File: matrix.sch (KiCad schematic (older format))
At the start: 143 parts

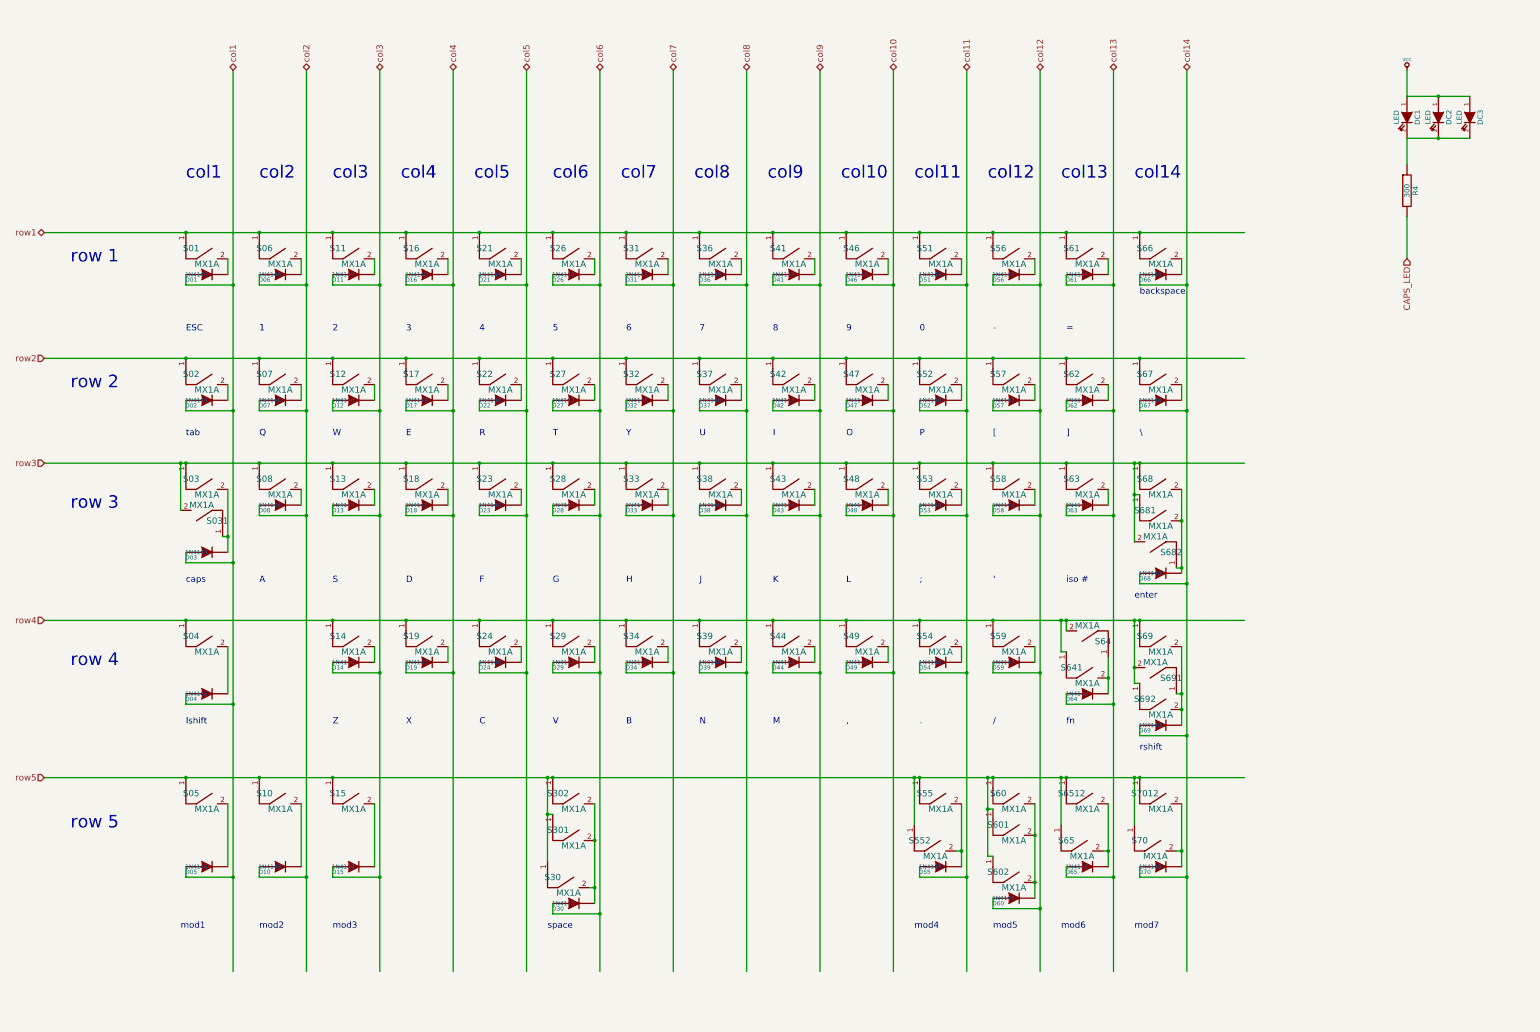
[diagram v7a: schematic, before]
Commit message: Remove unnecessary caps SW and related leds
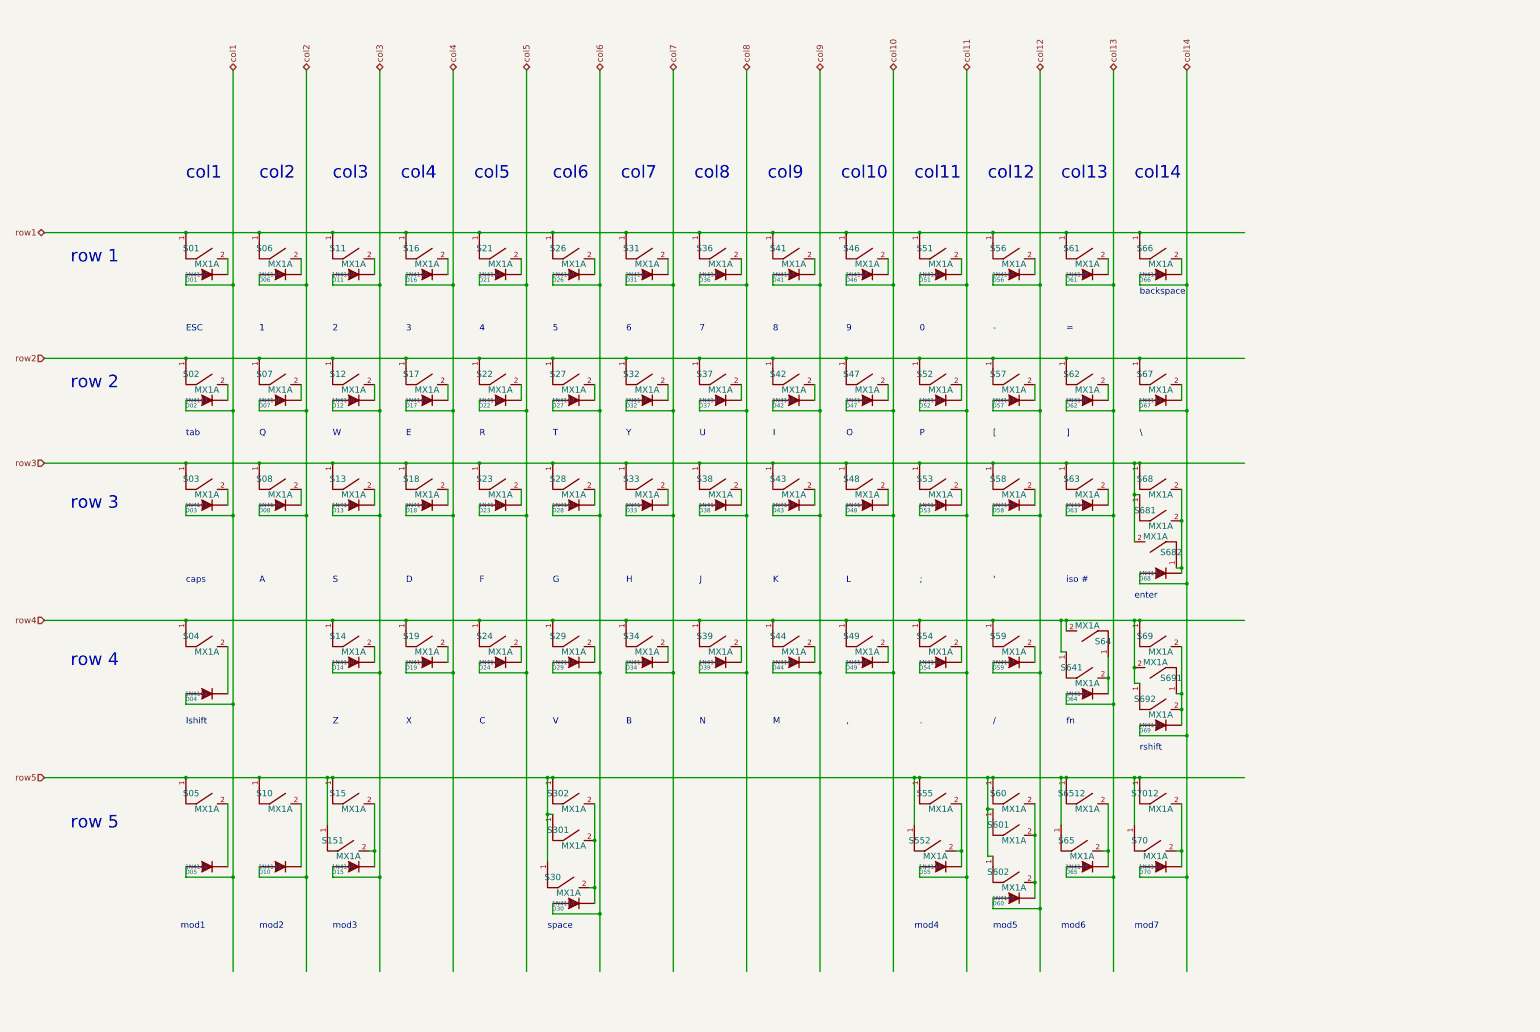
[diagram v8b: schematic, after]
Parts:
- removed DC1, DC2: LED, mx1a:MX1A-led_no3d, symbol device:LED
- removed DC3: LED, symbol device:LED
- removed R4: 300, symbol device:R
- removed S031: MX1A, mx1a:MX1A_no3d, symbol mx1a-simple:MX1A
- added S151: MX1A, mx1a:MX1A_no3d, symbol mx1a-simple:MX1A
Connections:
- net labels removed: CAPS_LED, VCC
- wire segments 390 -> 383
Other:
- moved on the sheet: D03
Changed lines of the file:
@@
 Text Notes 8000 2450 0    120  ~ 0
 col8
-$Comp
-L mx1a-simple:MX1A S031
-U 1 1 5042A9E4
-P 3300 5450
-F 0 "S031" H 3150 5700 60  0000 C CNN
-F 1 "MX1A" H 3300 5550 60  0000 C CNN
-F 2 "mx1a:MX1A_no3d" H 3300 5450 60  0001 C CNN
-F 3 "" H 3300 5450 60  0001 C CNN
-	1    3300 5450
-	-1   0    0    1
-$EndComp
-$Comp
-L device:LED DC1
-U 1 1 5042BB59
-P 14800 1850
-F 0 "DC1" H 14800 1950 50  0000 C CNN
-F 1 "LED" H 14800 1750 50  0000 C CNN
-F 2 "mx1a:MX1A-led_no3d" H 14800 1850 60  0001 C CNN
-F 3 "" H 14800 1850 60  0001 C CNN
-	1    14800 1850
-	0    1    1    0
-$EndComp
-$Comp
-L device:LED DC2
-U 1 1 5042BEB0
-P 15100 1850
-F 0 "DC2" H 15100 1950 50  0000 C CNN
-F 1 "LED" H 15100 1750 50  0000 C CNN
-F 2 "mx1a:MX1A-led_no3d" H 15100 1850 60  0001 C CNN
-F 3 "" H 15100 1850 60  0001 C CNN
-	1    15100 1850
-	0    1    1    0
-$EndComp
 Text HLabel 1800 2950 0    60   3State ~ 0
 row1
@@
 col14
 $Comp
-L power1:VCC #PWR031
-U 1 1 5043970C
-P 14800 1400
-F 0 "#PWR031" H 14800 1500 30  0001 C CNN
-F 1 "VCC" H 14800 1500 30  0000 C CNN
-F 2 "" H 14800 1400 60  0001 C CNN
-F 3 "" H 14800 1400 60  0001 C CNN
-	1    14800 1400
-	1    0    0    -1
-$EndComp
-$Comp
-L device:R R4
-U 1 1 5043A0D0
-P 14800 2550
-F 0 "R4" V 14880 2550 50  0000 C CNN
-F 1 "300" V 14800 2550 50  0000 C CNN
-F 2 "" H 14800 2550 60  0001 C CNN
-F 3 "" H 14800 2550 60  0001 C CNN
-	1    14800 2550
-	1    0    0    -1
-$EndComp
-Text HLabel 14800 3200 3    60   Input ~ 0
-CAPS_LED
-$Comp
 L mx1a-simple:MX1A S41
 U 1 1 5040DDC7
@@
 L device:DIODE D03
 U 1 1 506B5DE9
-P 3350 6000
-F 0 "D03" H 3200 5950 40  0000 C CNN
-F 1 "1N4148" H 3250 6000 40  0000 C CNN
-F 2 "0805:0805D" H 3350 6000 60  0001 C CNN
-F 3 "" H 3350 6000 60  0001 C CNN
-F 4 "DC Components" H 3350 4350 60  0001 C CNN "Vendor"
-F 5 "CD4148WS(0805C)" H 3350 4350 60  0001 C CNN "Product"
-F 6 "TME" H 3350 4350 60  0001 C CNN "Supplier"
-F 7 "1N4148-0805" H 3350 4350 60  0001 C CNN "Supplier Symbol"
-	1    3350 6000
-	1    0    0    -1
-$EndComp
-$Comp
-L device:LED DC3
-U 1 1 506E072F
-P 15400 1850
-F 0 "DC3" H 15400 1950 50  0000 C CNN
-F 1 "LED" H 15400 1750 50  0000 C CNN
-F 2 "" H 15400 1850 60  0001 C CNN
-F 3 "" H 15400 1850 60  0001 C CNN
-	1    15400 1850
-	0    1    1    0
+P 3350 5550
+F 0 "D03" H 3200 5500 40  0000 C CNN
+F 1 "1N4148" H 3250 5550 40  0000 C CNN
+F 2 "0805:0805D" H 3350 5550 60  0001 C CNN
+F 3 "" H 3350 5550 60  0001 C CNN
+F 4 "DC Components" H 3350 3900 60  0001 C CNN "Vendor"
+F 5 "CD4148WS(0805C)" H 3350 3900 60  0001 C CNN "Product"
+F 6 "TME" H 3350 3900 60  0001 C CNN "Supplier"
+F 7 "1N4148-0805" H 3350 3900 60  0001 C CNN "Supplier Symbol"
+	1    3350 5550
+	1    0    0    -1
 $EndComp
 $Comp
@@
 Connection ~ 11250 8700
 Wire Wire Line
-	1800 5150 3100 5150
-Wire Wire Line
 	5000 1400 5000 3450
 Wire Wire Line
@@
 Wire Wire Line
 	7050 9200 7000 9200
-Wire Wire Line
-	3100 5150 3100 5600
-Connection ~ 3100 5150
-Wire Wire Line
-	3550 5400 3550 5850
-Wire Wire Line
-	3550 5850 3500 5850
-Wire Wire Line
-	14800 1400 14800 1650
-Wire Wire Line
-	14800 1650 15100 1650
-Wire Wire Line
-	14800 2050 15100 2050
-Wire Wire Line
-	14800 2050 14800 2300
-Wire Wire Line
-	14800 2800 14800 3200
 Wire Wire Line
 	12200 6650 12200 7100
@@
 Connection ~ 7050 9200
 Wire Wire Line
-	3150 6000 3150 6100
-Wire Wire Line
-	3150 6100 3600 6100
+	3150 5550 3150 5650
+Wire Wire Line
+	3150 5650 3600 5650
 Connection ~ 3600 3450
 Connection ~ 4300 3450
@@
 Connection ~ 4300 4650
 Connection ~ 3600 4650
-Connection ~ 3600 6100
 Connection ~ 4300 5650
 Connection ~ 5000 5650
@@
 Connection ~ 12650 5700
 Connection ~ 11950 7200
-Connection ~ 3550 5850
 Connection ~ 9450 5150
 Connection ~ 9450 4150
 Connection ~ 9450 2950
-Connection ~ 15100 1650
-Connection ~ 15100 2050
 Wire Wire Line
 	12250 6300 12250 6200
@@
 	6600 8150 6650 8150
 Wire Wire Line
-	3100 5150 3150 5150
-Wire Wire Line
 	12200 6650 12250 6650
 Wire Wire Line
@@
 	4300 4650 4300 5650
 Wire Wire Line
-	3600 4650 3600 6100
+	3600 4650 3600 5650
 Wire Wire Line
 	5000 5650 5000 7150
@@
 	11950 7200 11950 7350
 Wire Wire Line
-	3550 5850 3550 6000
-Wire Wire Line
 	9450 5150 10150 5150
 Wire Wire Line
@@
 Wire Wire Line
 	9450 2950 10150 2950
-Wire Wire Line
-	15100 1650 15400 1650
-Wire Wire Line
-	15100 2050 15400 2050
 Wire Wire Line
 	12200 5450 12200 5900
@@
 Wire Wire Line
 	3600 7450 3600 9100
-Wire Wire Line
-	3600 6100 3600 7450
 Connection ~ 3600 7450
 Wire Wire Line
@@
 	4300 9100 4300 10000
 Wire Wire Line
-	3850 8150 4550 8150
-Wire Wire Line
-	4950 8400 4950 9000
+	4950 8850 4950 9000
+Wire Wire Line
+	4950 8400 4950 8850
+Connection ~ 4950 8850
+Wire Wire Line
+	4950 8850 4900 8850
+Wire Wire Line
+	3850 8150 4500 8150
+Wire Wire Line
+	4500 8150 4550 8150
+Connection ~ 4500 8150
+Wire Wire Line
+	4500 8150 4500 8600
+$Comp
+L mx1a-simple:MX1A S151
+U 1 1 5040F14F
+P 4700 9000
+F 0 "S151" H 4550 9250 60  0000 C CNN
+F 1 "MX1A" H 4700 9100 60  0000 C CNN
+F 2 "mx1a:MX1A_no3d" H 4700 9000 60  0001 C CNN
+F 3 "" H 4700 9000 60  0001 C CNN
+	1    4700 9000
+	1    0    0    -1
+$EndComp
+Wire Wire Line
+	1800 5150 3150 5150
+Wire Wire Line
+	3550 5400 3550 5550
+Connection ~ 3600 5650
+Wire Wire Line
+	3600 5650 3600 7450
 $EndSCHEMATC
